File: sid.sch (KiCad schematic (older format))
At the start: 40 parts, among them CN11 CONN_SID_OUTPUT, CN12 CONN_SID_INPUT, J1 CONN_JOY3, Q6 2SC1815, SW2 SW_DIGIFIX, U21 74LS04, U24 MOS_8580, U25 74LS74, U27 74HCT245

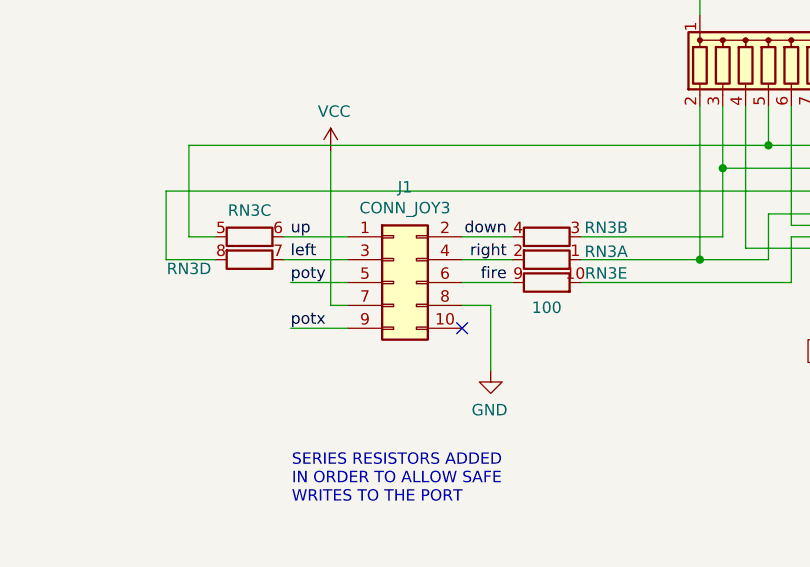
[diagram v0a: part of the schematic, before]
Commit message: J1 -> CN14
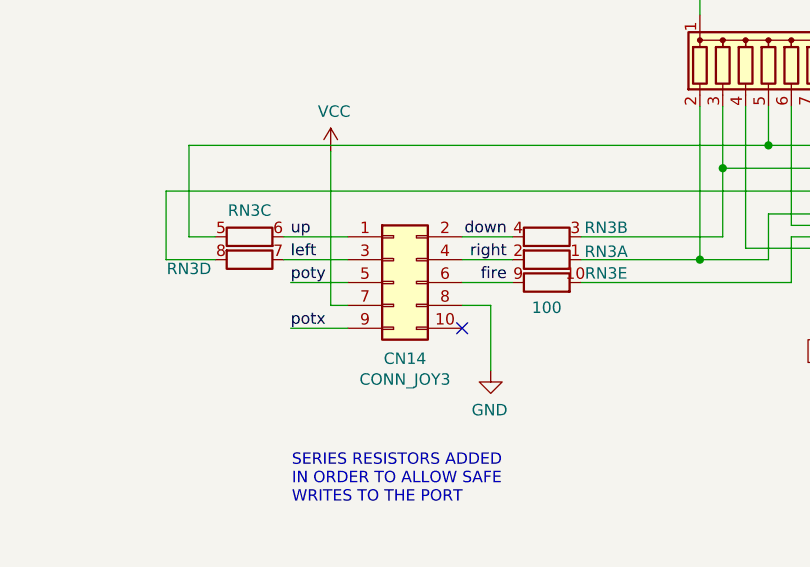
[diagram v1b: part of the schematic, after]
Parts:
- renumbered J1 to CN14
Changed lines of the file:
@@
 $EndComp
 $Comp
-L Connector_Generic:Conn_02x05_Odd_Even J1
+L Connector_Generic:Conn_02x05_Odd_Even CN14
 U 1 1 64DAD690
 P 11250 6855
-F 0 "J1" H 11300 7272 50  0000 C CNN
-F 1 "CONN_JOY3" H 11300 7181 50  0000 C CNN
+F 0 "CN14" H 11300 6522 50  0000 C CNN
+F 1 "CONN_JOY3" H 11300 6431 50  0000 C CNN
 F 2 "Connector_PinHeader_2.54mm:PinHeader_2x05_P2.54mm_Vertical" H 11250 6855 50  0001 C CNN
 F 3 "~" H 11250 6855 50  0001 C CNN

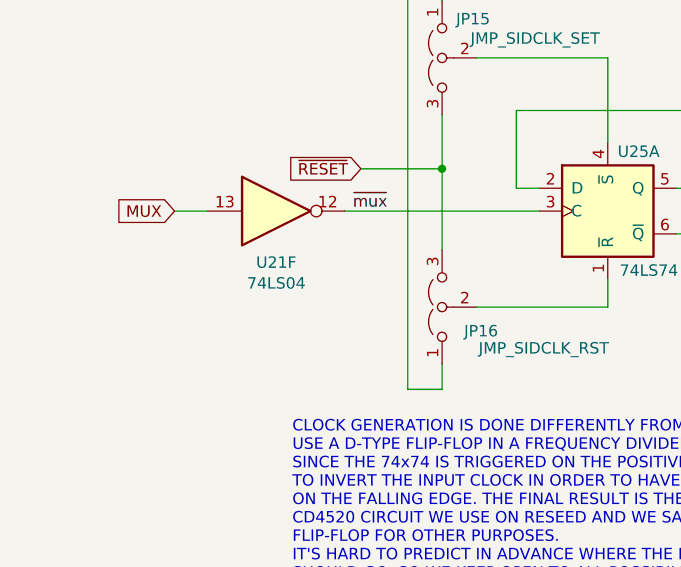
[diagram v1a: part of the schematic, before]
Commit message: U21 -> HCT
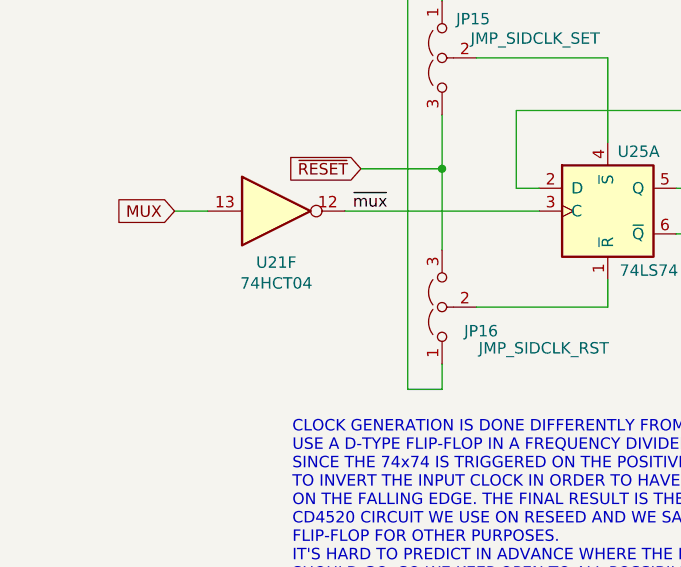
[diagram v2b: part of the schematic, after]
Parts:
- U21: value 74LS04 -> 74HCT04
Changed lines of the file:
@@
 AR Path="/64A6E6F3/64BD3AD0" Ref="U21"  Part="6"
 F 0 "U21" H 1765 6245 50  0000 C CNN
-F 1 "74LS04" H 1765 6154 50  0000 C CNN
+F 1 "74HCT04" H 1765 6154 50  0000 C CNN
 F 2 "LittleSixteen:DIP-14_W7.62mm_Socket_LongPads" H 1765 6470 50  0001 C CNN
 F 3 "http://www.ti.com/lit/gpn/sn74LS04" H 1765 6470 50  0001 C CNN

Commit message: Add ROM bank switcher (All-in-one ROM only)
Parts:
- RV3, RV4: footprint LittleSixteen:Pot_Bourns_3306P -> Potentiometer_THT:Potentiometer_Bourns_3296W_Vertical
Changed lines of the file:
@@
 F 0 "RV3" H 13280 2034 50  0000 R CNN
 F 1 "10k" H 13280 2125 50  0000 R CNN
-F 2 "LittleSixteen:Pot_Bourns_3306P" H 13350 2080 50  0001 C CNN
+F 2 "Potentiometer_THT:Potentiometer_Bourns_3296W_Vertical" H 13350 2080 50  0001 C CNN
 F 3 "~" H 13350 2080 50  0001 C CNN
 F 4 "652-3306P-1-103" H 13350 2080 50  0001 C CNN "MouserPN"
@@
 F 0 "RV4" V 11613 3625 50  0000 C CNN
 F 1 "1M" V 11704 3625 50  0000 C CNN
-F 2 "LittleSixteen:Pot_Bourns_3306P" H 11820 3625 50  0001 C CNN
+F 2 "Potentiometer_THT:Potentiometer_Bourns_3296W_Vertical" H 11820 3625 50  0001 C CNN
 F 3 "~" H 11820 3625 50  0001 C CNN
 F 4 "652-3306P-1-105" H 11820 3625 50  0001 C CNN "MouserPN"

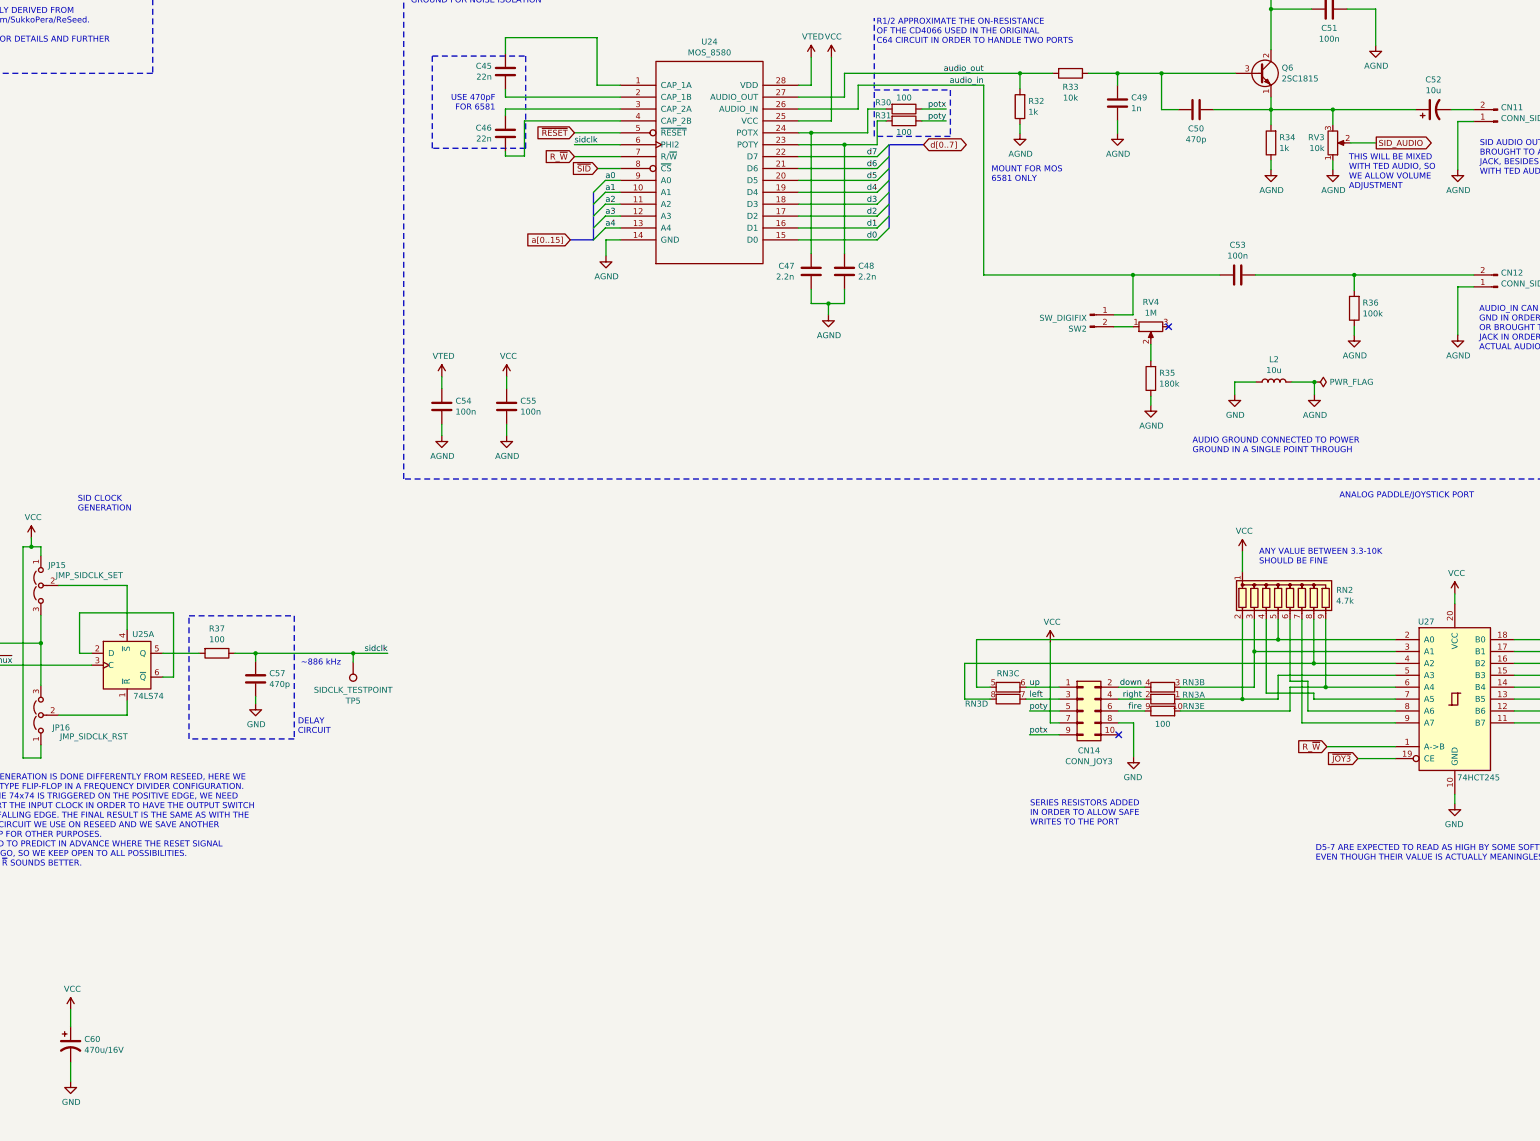
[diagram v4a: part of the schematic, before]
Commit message: Rationalize BOM There should be no significant changes on both schematics on PCB, just some values and something on the silkscreen
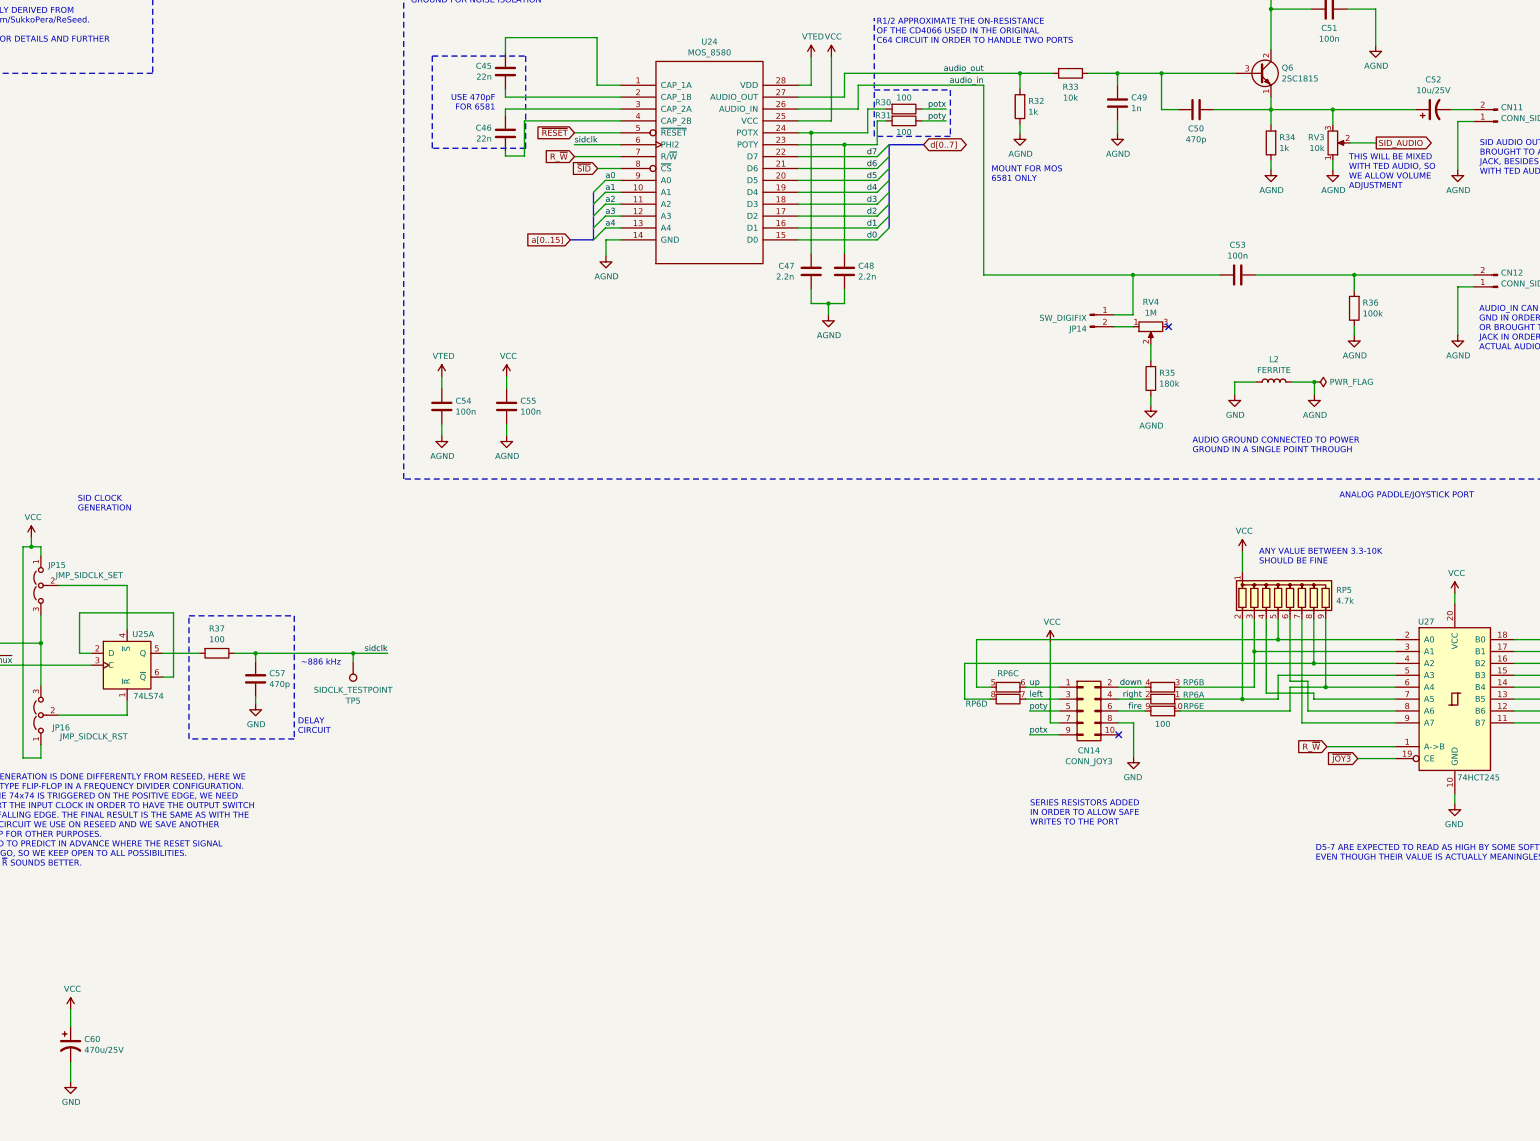
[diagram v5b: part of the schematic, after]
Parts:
- C52: value 10u -> 10u/25V
- C60: value 470u/16V -> 470u/25V; MouserPN 710-860020573008 -> 710-860010575013
- L2: value 10u -> FERRITE; MouserPN (none) -> 875-28C0236-0EW-10
- RP5: renamed from RN2; Notes (none) -> Bussed
- RP6: renamed from RN3; Notes (none) -> Isolated/Independent
- RV3: MouserPN 652-3306P-1-103 -> (none)
- RV4: MouserPN 652-3306P-1-105 -> (none)
- renumbered SW2 to JP14
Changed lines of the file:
@@
 P 14195 1800
 F 0 "C52" V 14447 1800 50  0000 C CNN
-F 1 "10u" V 14356 1800 50  0000 C CNN
+F 1 "10u/25V" V 14356 1800 50  0000 C CNN
 F 2 "Capacitor_THT:CP_Radial_D5.0mm_P2.00mm" H 14195 1800 50  0001 C CNN
 F 3 "~" H 14195 1800 50  0001 C CNN
@@
 F 2 "Potentiometer_THT:Potentiometer_Bourns_3296W_Vertical" H 13350 2080 50  0001 C CNN
 F 3 "~" H 13350 2080 50  0001 C CNN
-F 4 "652-3306P-1-103" H 13350 2080 50  0001 C CNN "MouserPN"
+F 4 "" H 13350 2080 50  0001 C CNN "MouserPN"
 F 5 "10k" H 13350 2080 50  0001 C CNN "Value"
 	1    13350 2080
@@
 AR Path="/64A6E6F3/65CC3782" Ref="L2"  Part="1"
 F 0 "L2" V 13045 4090 50  0000 C CNN
-F 1 "10u" V 12954 4090 50  0000 C CNN
+F 1 "FERRITE" V 12954 4090 50  0000 C CNN
 F 2 "Inductor_THT:L_Radial_D6.0mm_P4.00mm" H 12855 4090 50  0001 C CNN
 F 3 "~" H 12855 4090 50  0001 C CNN
+F 4 "875-28C0236-0EW-10" H 12855 4090 50  0001 C CNN "MouserPN"
 	1    12855 4090
 	0    -1   -1   0
@@
 $EndComp
 $Comp
-L Device:R_Network08 RN2
+L Device:R_Network08 RP5
 U 1 1 64D2E526
 P 12990 5885
-F 0 "RN2" H 13378 5931 50  0000 L CNN
+F 0 "RP5" H 13378 5931 50  0000 L CNN
 F 1 "4.7k" H 13378 5840 50  0000 L CNN
 F 2 "Resistor_THT:R_Array_SIP9" V 13465 5885 50  0001 C CNN
 F 3 "http://www.vishay.com/docs/31509/csc.pdf" H 12990 5885 50  0001 C CNN
+F 4 "Bussed" H 12990 5885 50  0001 C CNN "Notes"
 	1    12990 5885
 	1    0    0    -1
@@
 $EndComp
 $Comp
-L Device:R_Pack05_SIP_Split RN3
+L Device:R_Pack05_SIP_Split RP6
 U 4 1 63A29AC0
 P 10620 6755
-F 0 "RN3" V 10580 7020 50  0000 C CNN
+F 0 "RP6" V 10580 7020 50  0000 C CNN
 F 1 "100" H 10708 6710 50  0001 L CNN
 F 2 "Resistor_THT:R_Array_SIP10" V 10540 6755 50  0001 C CNN
@@
 F 4 "652-4610X-2LF-100" H 10620 6755 50  0001 C CNN "MouserPN"
 F 5 "100" H 10620 6755 50  0001 C CNN "Value"
+F 6 "Isolated/Independent" H 10620 6755 50  0001 C CNN "Notes"
 	4    10620 6755
 	0    -1   -1   0
 $EndComp
 $Comp
-L Device:R_Pack05_SIP_Split RN3
+L Device:R_Pack05_SIP_Split RP6
 U 5 1 63A26FF8
 P 11920 6855
-F 0 "RN3" V 11880 7115 50  0000 C CNN
+F 0 "RP6" V 11880 7115 50  0000 C CNN
 F 1 "100" V 12030 6855 50  0000 C CNN
 F 2 "Resistor_THT:R_Array_SIP10" V 11840 6855 50  0001 C CNN
@@
 F 4 "652-4610X-2LF-100" H 11920 6855 50  0001 C CNN "MouserPN"
 F 5 "100" H 11920 6855 50  0001 C CNN "Value"
+F 6 "Isolated/Independent" H 11920 6855 50  0001 C CNN "Notes"
 	5    11920 6855
 	0    1    1    0
 $EndComp
 $Comp
-L Device:R_Pack05_SIP_Split RN3
+L Device:R_Pack05_SIP_Split RP6
 U 3 1 63A27F03
 P 10620 6655
-F 0 "RN3" V 10505 6655 50  0000 C CNN
+F 0 "RP6" V 10505 6655 50  0000 C CNN
 F 1 "100" V 10504 6655 50  0001 C CNN
 F 2 "Resistor_THT:R_Array_SIP10" V 10540 6655 50  0001 C CNN
@@
 F 4 "652-4610X-2LF-100" H 10620 6655 50  0001 C CNN "MouserPN"
 F 5 "100" H 10620 6655 50  0001 C CNN "Value"
+F 6 "Isolated/Independent" H 10620 6655 50  0001 C CNN "Notes"
 	3    10620 6655
 	0    1    1    0
 $EndComp
 $Comp
-L Device:R_Pack05_SIP_Split RN3
+L Device:R_Pack05_SIP_Split RP6
 U 2 1 63A28C60
 P 11920 6655
-F 0 "RN3" V 11880 6395 50  0000 C CNN
+F 0 "RP6" V 11880 6395 50  0000 C CNN
 F 1 "100" V 11804 6655 50  0001 C CNN
 F 2 "Resistor_THT:R_Array_SIP10" V 11840 6655 50  0001 C CNN
@@
 F 4 "652-4610X-2LF-100" H 11920 6655 50  0001 C CNN "MouserPN"
 F 5 "100" H 11920 6655 50  0001 C CNN "Value"
+F 6 "Isolated/Independent" H 11920 6655 50  0001 C CNN "Notes"
 	2    11920 6655
 	0    -1   1    0
 $EndComp
 $Comp
-L Device:R_Pack05_SIP_Split RN3
+L Device:R_Pack05_SIP_Split RP6
 U 1 1 63A2AA82
 P 11920 6755
-F 0 "RN3" V 11955 6495 50  0000 C CNN
+F 0 "RP6" V 11955 6495 50  0000 C CNN
 F 1 "100" H 12008 6710 50  0001 L CNN
 F 2 "Resistor_THT:R_Array_SIP10" V 11840 6755 50  0001 C CNN
@@
 F 4 "652-4610X-2LF-100" H 11920 6755 50  0001 C CNN "MouserPN"
 F 5 "100" H 11920 6755 50  0001 C CNN "Value"
+F 6 "Isolated/Independent" H 11920 6755 50  0001 C CNN "Notes"
 	1    11920 6755
 	0    -1   -1   0
@@
 F 2 "Potentiometer_THT:Potentiometer_Bourns_3296W_Vertical" H 11820 3625 50  0001 C CNN
 F 3 "~" H 11820 3625 50  0001 C CNN
-F 4 "652-3306P-1-105" H 11820 3625 50  0001 C CNN "MouserPN"
+F 4 "" H 11820 3625 50  0001 C CNN "MouserPN"
 F 5 "For 6581 do not mount" H 11820 3625 50  0001 C CNN "Notes"
 F 6 "1M" H 11820 3625 50  0001 C CNN "Value"
@@
 P 2740 9660
 F 0 "C60" H 2855 9706 50  0000 L CNN
-F 1 "470u/16V" H 2855 9615 50  0000 L CNN
+F 1 "470u/25V" H 2855 9615 50  0000 L CNN
 F 2 "Capacitor_THT:CP_Radial_D10.0mm_P5.00mm" H 2740 9660 50  0001 C CNN
 F 3 "~" H 2740 9660 50  0001 C CNN
-F 4 "710-860020573008" H 2740 9660 50  0001 C CNN "MouserPN"
+F 4 "710-860010575013" H 2740 9660 50  0001 C CNN "MouserPN"
 F 5 "100u/16V" H 2740 9660 50  0001 C CNN "Value"
 	1    2740 9660
@@
 	11510 3525 11670 3525
 $Comp
-L Connector:Conn_01x02_Male SW2
+L Connector:Conn_01x02_Male JP14
 U 1 1 652F59B8
 P 11310 3525
-F 0 "SW2" H 11282 3407 50  0000 R CNN
+F 0 "JP14" H 11282 3407 50  0000 R CNN
 F 1 "SW_DIGIFIX" H 11282 3498 50  0000 R CNN
 F 2 "Connector_PinHeader_2.54mm:PinHeader_1x02_P2.54mm_Vertical" H 11310 3525 50  0001 C CNN

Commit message: Rationalize capacitor footprints & BOM
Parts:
- C52: MouserPN 710-860010472002 -> 710-860010672009
- C60: footprint Capacitor_THT:CP_Radial_D10.0mm_P5.00mm -> Capacitor_THT:CP_Radial_D8.0mm_P3.50mm; MouserPN 710-860010575013 -> 710-860010474013
- R30, R31, R37: MouserPN 660-MF1/4LCT52R101G -> 708-RNF14FTD100R
- RV3: MouserPN (none) -> 652-3296W-1-103LF
- RV4: MouserPN (none) -> 652-3296W-1-105LF
- TP5: MouserPN (none) -> ---
- U27: MouserPN 595-SN74HCT245N -> 595-SN74HCT245ANSR; Notes (none) -> Or 595-SN74HCT245NE4
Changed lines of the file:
@@
 F 2 "Capacitor_THT:CP_Radial_D5.0mm_P2.00mm" H 14195 1800 50  0001 C CNN
 F 3 "~" H 14195 1800 50  0001 C CNN
-F 4 "710-860010472002" H 14195 1800 50  0001 C CNN "MouserPN"
+F 4 "710-860010672009" H 14195 1800 50  0001 C CNN "MouserPN"
 F 5 "10u" H 14195 1800 50  0001 C CNN "Value"
 	1    14195 1800
@@
 F 2 "Potentiometer_THT:Potentiometer_Bourns_3296W_Vertical" H 13350 2080 50  0001 C CNN
 F 3 "~" H 13350 2080 50  0001 C CNN
-F 4 "" H 13350 2080 50  0001 C CNN "MouserPN"
+F 4 "652-3296W-1-103LF" H 13350 2080 50  0001 C CNN "MouserPN"
 F 5 "10k" H 13350 2080 50  0001 C CNN "Value"
 	1    13350 2080
@@
 F 2 "Resistor_THT:R_Axial_DIN0207_L6.3mm_D2.5mm_P5.08mm_Vertical" V 3900 6370 50  0001 C CNN
 F 3 "~" H 3970 6370 50  0001 C CNN
-F 4 "660-MF1/4LCT52R101G" H 3970 6370 50  0001 C CNN "MouserPN"
+F 4 "708-RNF14FTD100R" H 3970 6370 50  0001 C CNN "MouserPN"
 F 5 "" H 3970 6370 50  0001 C CNN "Notes"
 F 6 "100" H 3970 6370 50  0001 C CNN "Value"
@@
 F 2 "LittleSixteen:DIP-20_W7.62mm_Socket_LongPads" H 14375 6755 50  0001 C CNN
 F 3 "http://www.ti.com/lit/gpn/sn74LS245" H 14375 6755 50  0001 C CNN
-F 4 "595-SN74HCT245N" H 14375 6755 50  0001 C CNN "MouserPN"
+F 4 "595-SN74HCT245ANSR" H 14375 6755 50  0001 C CNN "MouserPN"
 F 5 "74HCT245" H 14375 6755 50  0001 C CNN "Value"
+F 6 "Or 595-SN74HCT245NE4" H 14375 6755 50  0001 C CNN "Notes"
 	1    14375 6755
 	1    0    0    -1
@@
 F 2 "Potentiometer_THT:Potentiometer_Bourns_3296W_Vertical" H 11820 3625 50  0001 C CNN
 F 3 "~" H 11820 3625 50  0001 C CNN
-F 4 "" H 11820 3625 50  0001 C CNN "MouserPN"
+F 4 "652-3296W-1-105LF" H 11820 3625 50  0001 C CNN "MouserPN"
 F 5 "For 6581 do not mount" H 11820 3625 50  0001 C CNN "Notes"
 F 6 "1M" H 11820 3625 50  0001 C CNN "Value"
@@
 F 0 "C60" H 2855 9706 50  0000 L CNN
 F 1 "470u/25V" H 2855 9615 50  0000 L CNN
-F 2 "Capacitor_THT:CP_Radial_D10.0mm_P5.00mm" H 2740 9660 50  0001 C CNN
+F 2 "Capacitor_THT:CP_Radial_D8.0mm_P3.50mm" H 2740 9660 50  0001 C CNN
 F 3 "~" H 2740 9660 50  0001 C CNN
-F 4 "710-860010575013" H 2740 9660 50  0001 C CNN "MouserPN"
+F 4 "710-860010474013" H 2740 9660 50  0001 C CNN "MouserPN"
 F 5 "100u/16V" H 2740 9660 50  0001 C CNN "Value"
 	1    2740 9660
@@
 F 2 "Resistor_THT:R_Axial_DIN0207_L6.3mm_D2.5mm_P5.08mm_Vertical" V 9675 1795 50  0001 C CNN
 F 3 "~" H 9745 1795 50  0001 C CNN
-F 4 "660-MF1/4LCT52R101G" H 9745 1795 50  0001 C CNN "MouserPN"
+F 4 "708-RNF14FTD100R" H 9745 1795 50  0001 C CNN "MouserPN"
 F 5 "100" H 9745 1795 50  0001 C CNN "Value"
 	1    9745 1795
@@
 F 2 "Resistor_THT:R_Axial_DIN0207_L6.3mm_D2.5mm_P5.08mm_Vertical" V 9675 1895 50  0001 C CNN
 F 3 "~" H 9745 1895 50  0001 C CNN
-F 4 "660-MF1/4LCT52R101G" H 9745 1895 50  0001 C CNN "MouserPN"
+F 4 "708-RNF14FTD100R" H 9745 1895 50  0001 C CNN "MouserPN"
 F 5 "100" H 9745 1895 50  0001 C CNN "Value"
 	1    9745 1895
@@
 F 2 "TestPoint:TestPoint_Pad_D2.0mm" H 5315 6445 50  0001 C CNN
 F 3 "~" H 5315 6445 50  0001 C CNN
+F 4 "---" H 5115 6445 50  0001 C CNN "MouserPN"
 	1    5115 6445
 	-1   0    0    1

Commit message: Add note on some components
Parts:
- C45, C46: Notes For 6581 use 470pF -> For 6581 use 470pF, polyester film cap recommended
- C52: Notes (none) -> Audio cap recommended
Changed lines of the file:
@@
 F 4 "710-860010672009" H 14195 1800 50  0001 C CNN "MouserPN"
 F 5 "10u" H 14195 1800 50  0001 C CNN "Value"
+F 6 "Audio cap recommended" H 14195 1800 50  0001 C CNN "Notes"
 	1    14195 1800
 	0    -1   -1   0
@@
 F 3 "~" H 6395 2000 50  0001 C CNN
 F 4 "810-FG28X7R1H223KNT0" H 6395 2000 50  0001 C CNN "MouserPN"
-F 5 "For 6581 use 470pF" H 6395 2000 50  0001 C CNN "Notes"
+F 5 "For 6581 use 470pF, polyester film cap recommended" H 6395 2000 50  0001 C CNN "Notes"
 F 6 "22n" H 6395 2000 50  0001 C CNN "Value"
 	1    6395 2000
@@
 F 3 "~" H 6395 1480 50  0001 C CNN
 F 4 "810-FG28X7R1H223KNT0" H 6395 1480 50  0001 C CNN "MouserPN"
-F 5 "For 6581 use 470pF" H 6395 1480 50  0001 C CNN "Notes"
+F 5 "For 6581 use 470pF, polyester film cap recommended" H 6395 1480 50  0001 C CNN "Notes"
 F 6 "22n" H 6395 1480 50  0001 C CNN "Value"
 	1    6395 1480
